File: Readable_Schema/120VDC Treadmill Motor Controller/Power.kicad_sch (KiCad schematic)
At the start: 4 parts, among them J1 Conn_01x02_Pin, K1 T9GV1L14-5, U8 RAC05E-05SKT

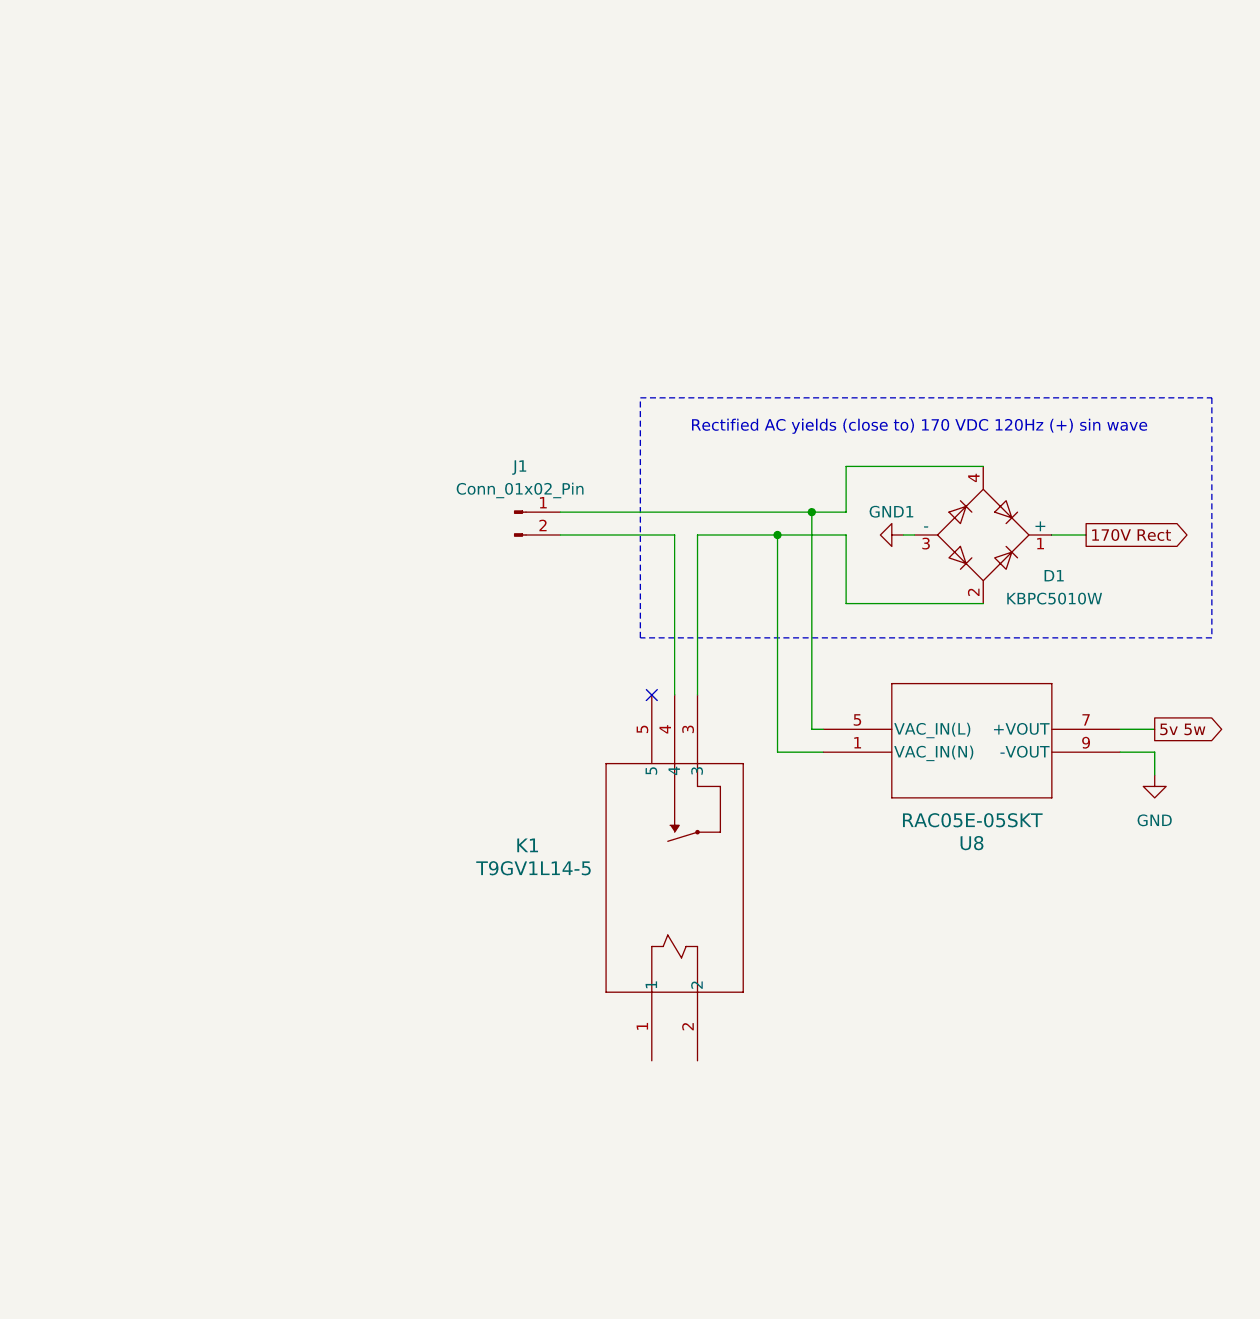
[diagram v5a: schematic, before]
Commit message: Finished adding e stop circuit and roughly choosing a cap for high voltage line -- mostly to deal with ripple current. Almost done implementing the brake resistor subcircuit
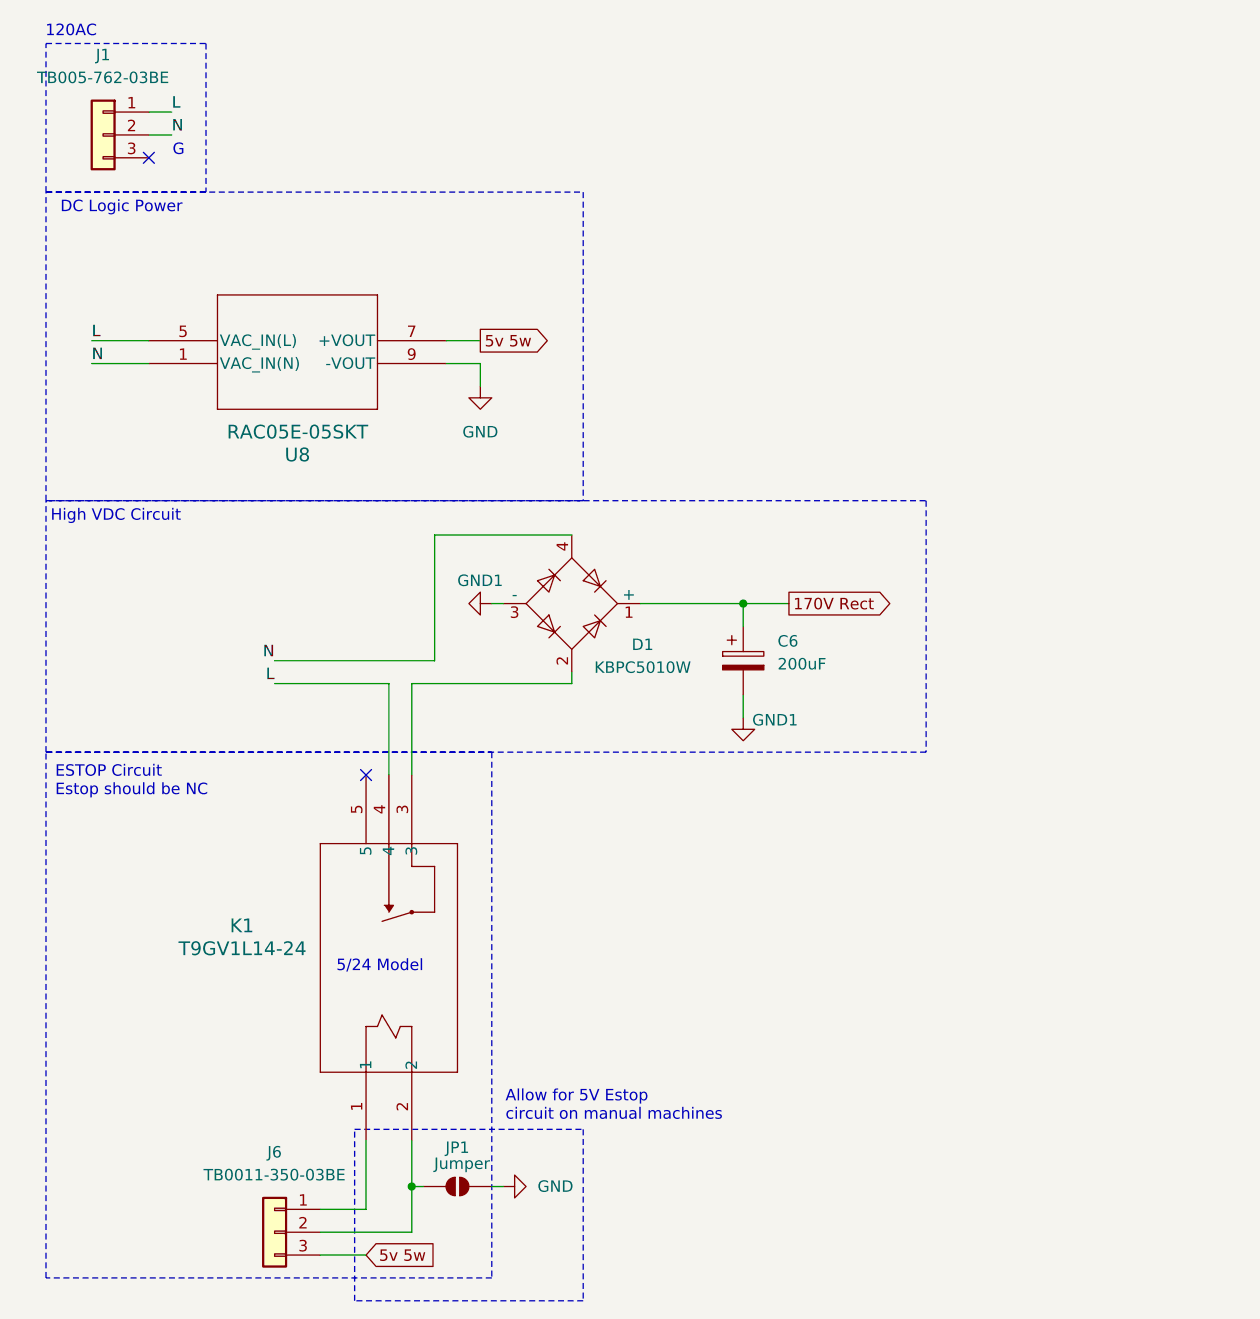
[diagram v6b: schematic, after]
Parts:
- removed J1: Conn_01x02_Pin, symbol Connector:Conn_01x02_Pin
- added C6: 200uF, Capacitor_THT:CP_Radial_D18.0mm_P7.50mm, symbol Device:C_Polarized
- added J1: TB005-762-03BE, Treadmill_Feet:CUI_TB005_-762-03BE, symbol Connector_Generic:Conn_01x03
- added J6: TB0011-350-03BE, symbol Connector_Generic:Conn_01x03
- added JP1: Jumper, symbol Jumper:SolderJumper_2_Open
- K1: value T9GV1L14-5 -> T9GV1L14-24
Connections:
- net 170V Rect: now also C6.1
- net 5v 5w: now also J6.3 (Pin_3)
- net GND: now also JP1.2 (B)
- net GND1: now also C6.2
- net at K1.1: now also J6.1 (Pin_1)
- net at K1.2: now also J6.2 (Pin_2), JP1.1 (A)
- net at D1.2, K1.3: no longer U8.1 (VAC_IN(N))
- net L: now reaches K1.4
- net L: now also U8.5 (VAC_IN(L)), J1.1 (Pin_1)
- net N: now reaches D1.4
- net N: now also U8.1 (VAC_IN(N)), J1.2 (Pin_2); no longer U8.5 (VAC_IN(L))
- no-connect marks 1 -> 2
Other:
- note added: "120AC"
- note added: "5/24 Model"
- note added: "Allow for 5V Estop circuit on manual machines"
- note added: "DC Logic Power"
- note added: "ESTOP Circuit Estop should be NC"
- note added: "G"
- note added: "High VDC Circuit"
- note removed: "Rectified AC yields (close to) 170 VDC 120Hz (+) sin wave"
- moved on the sheet: D1, K1, U8

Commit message: we have reached the point of starting to roughly place where components should go (have not started messing with traces). -Confirm heatsink size so that we can block that area out on the schema -add some test points similar to what we were testing in ltspice to determine functionality of the device -Review general layout with dad to confirm we r good to start drawing traces
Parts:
- J6: footprint (none) -> Treadmill_Feet:SAMESKY_TB0011-350-03BE
- JP1: footprint (none) -> Jumper:SolderJumper-2_P1.3mm_Open_RoundedPad1.0x1.5mm
- K1: footprint T9GV1L14-5_TEC -> Treadmill_Feet:T9GV1L14-5_TEC
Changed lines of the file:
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@@
 			)
 		)
-		(property "Footprint" ""
+		(property "Footprint" "Treadmill_Feet:SAMESKY_TB0011-350-03BE"
 			(at 67.31 160.02 0)
 			(effects
@@
 			)
 		)
-		(property "Footprint" ""
+		(property "Footprint" "Jumper:SolderJumper-2_P1.3mm_Open_RoundedPad1.0x1.5mm"
 			(at 87.63 154.94 0)
 			(effects
@@
 			)
 		)
-		(property "Footprint" "T9GV1L14-5_TEC"
+		(property "Footprint" "Treadmill_Feet:T9GV1L14-5_TEC"
 			(at 77.47 149.86 0)
 			(effects

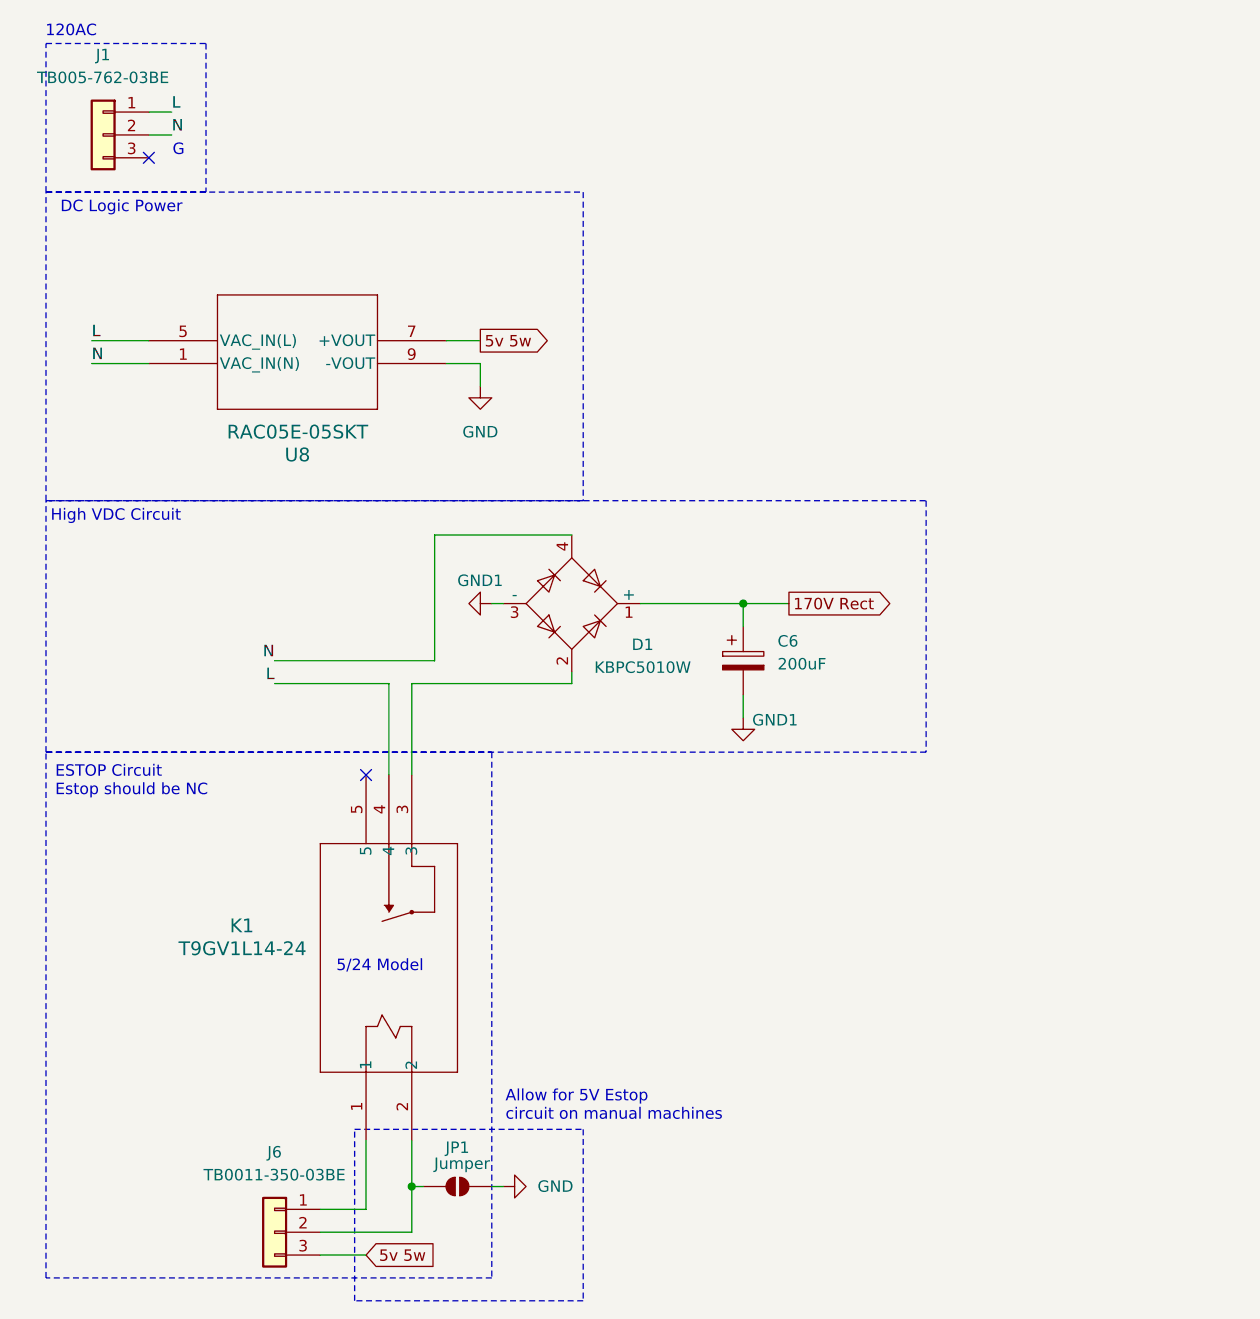
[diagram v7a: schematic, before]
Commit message: Changed ground naming and redid a bit of the pinouts between the pico and the h bridge -- need to fix the feedback loop to use a or gate for pwm_a and pwm_b to combine to one big reset
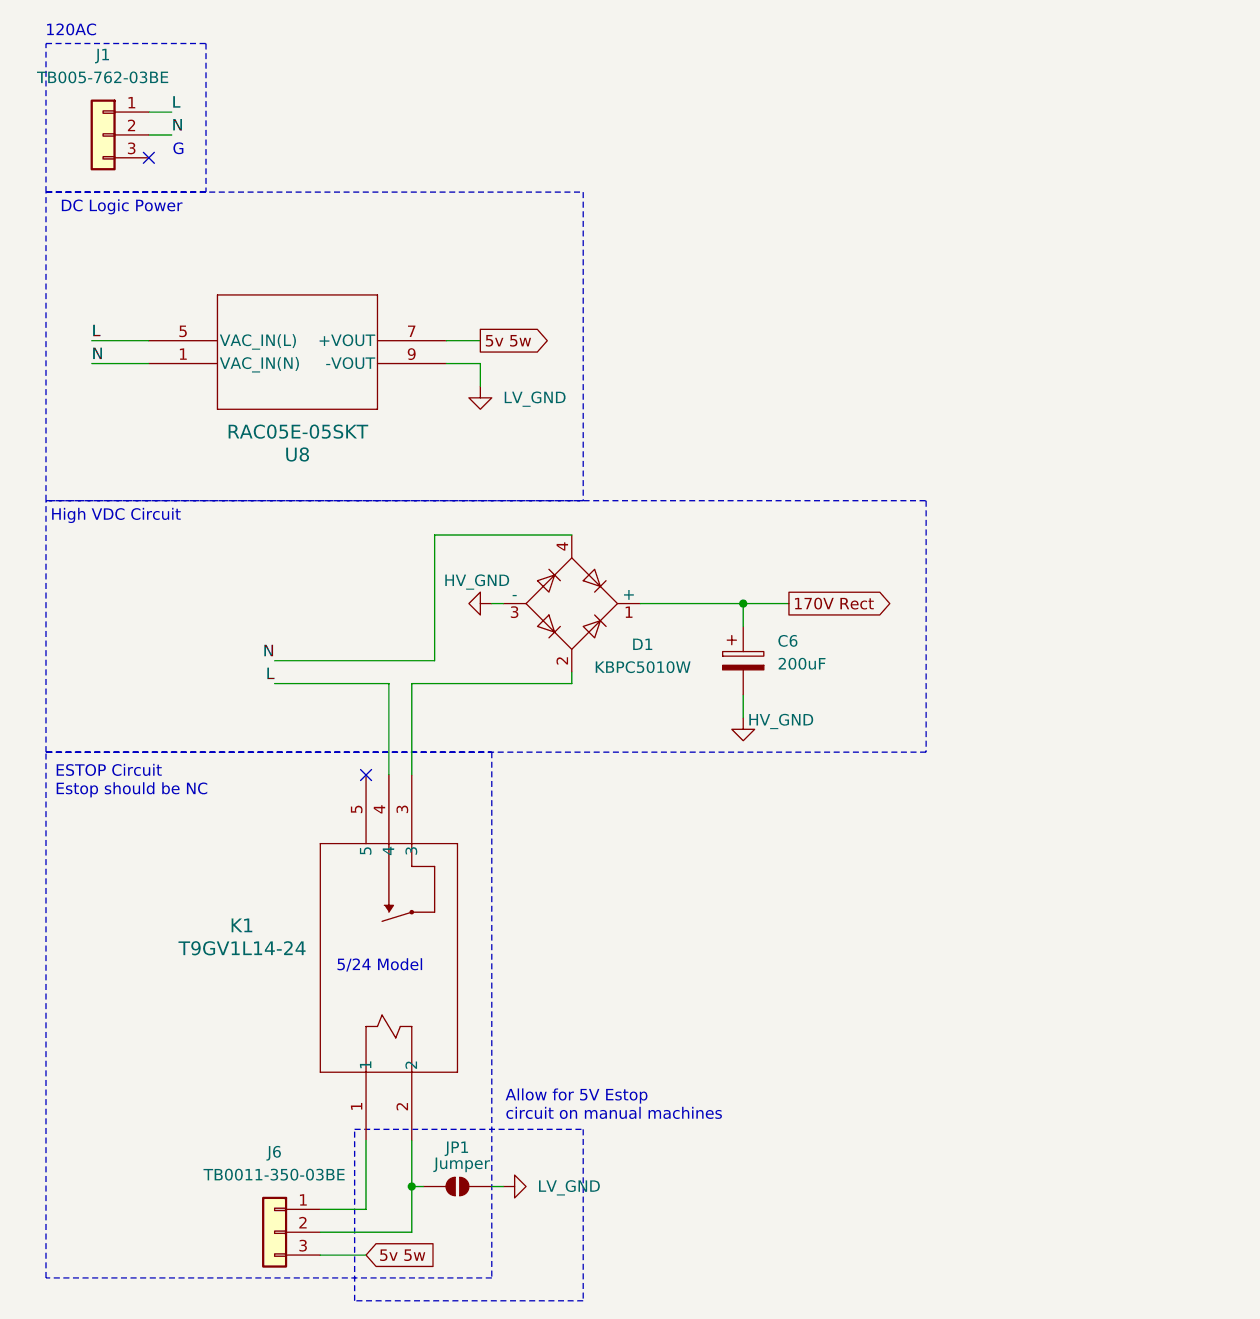
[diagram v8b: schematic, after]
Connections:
- net GND renamed LV_GND
- net GND1 renamed HV_GND
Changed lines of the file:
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@@
 			)
 		)
-		(property "Value" "GND"
-			(at 90.17 71.12 0)
-			(effects
-				(font
-					(size 1.27 1.27)
-				)
+		(property "Value" "LV_GND"
+			(at 92.71 67.3099 0)
+			(effects
+				(font
+					(size 1.27 1.27)
+				)
+				(justify left)
 			)
 		)
@@
 			)
 		)
-		(property "Value" "GND"
+		(property "Value" "LV_GND"
 			(at 96.52 154.9399 90)
 			(effects
@@
 			)
 		)
-		(property "Value" "GND1"
-			(at 125.476 103.124 0)
+		(property "Value" "HV_GND"
+			(at 127.254 103.124 0)
 			(effects
 				(font
@@
 			)
 		)
-		(property "Value" "GND1"
-			(at 92.71 87.63 90)
-			(effects
-				(font
+		(property "Value" "HV_GND"
+			(at 93.472 87.63 90)
+			(effects
+				(font
